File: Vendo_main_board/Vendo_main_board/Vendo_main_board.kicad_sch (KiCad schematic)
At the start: 8 parts, among them J1 Screw_Terminal_01x12, J2 Screw_Terminal_01x12, J3 Screw_Terminal_01x12, J4 Screw_Terminal_01x12

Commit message: -
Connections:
- net GNDPWR: now reaches J2.10 (Pin_10)
- net VIN+_REL_IN: now reaches J2.9 (Pin_9)
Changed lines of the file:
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@@
 		(color 0 0 0 0)
 	)
+	(junction
+		(at 302.827 226.1684)
+		(diameter 0)
+		(color 0 0 0 0)
+	)
 	(wire
 		(pts
@@
 	(wire
 		(pts
+			(xy 302.827 230.6876) (xy 302.827 226.1684)
+		)
+		(stroke
+			(width 0)
+			(type default)
+		)
+	)
+	(wire
+		(pts
 			(xy 245.3943 121.6976) (xy 314.8592 121.6976)
 		)
@@
 	(wire
 		(pts
+			(xy 300.3877 223.5894) (xy 339.8538 223.5894)
+		)
+		(stroke
+			(width 0)
+			(type default)
+		)
+	)
+	(wire
+		(pts
 			(xy 247.3131 77.6973) (xy 256.799 77.6973)
 		)
@@
 	(wire
 		(pts
+			(xy 302.827 226.1684) (xy 339.8538 226.1684)
+		)
+		(stroke
+			(width 0)
+			(type default)
+		)
+	)
+	(wire
+		(pts
 			(xy 193.24 61.42) (xy 193.24 104.1775)
 		)
@@
 	(wire
 		(pts
+			(xy 339.8538 226.1684) (xy 339.8538 226.1294)
+		)
+		(stroke
+			(width 0)
+			(type default)
+		)
+	)
+	(wire
+		(pts
 			(xy 341.3816 135.5405) (xy 341.3816 160.8719)
 		)
@@
 	(wire
 		(pts
+			(xy 300.4001 226.1684) (xy 302.827 226.1684)
+		)
+		(stroke
+			(width 0)
+			(type default)
+		)
+	)
+	(wire
+		(pts
 			(xy 109.0691 96.34) (xy 113.3814 96.34)
 		)
@@
 		)
 	)
+	(global_label "VIN+_REL_IN"
+		(shape input)
+		(at 300.3877 223.5894 180)
+		(fields_autoplaced yes)
+		(effects
+			(font
+				(size 1.27 1.27)
+			)
+			(justify right)
+		)
+		(property "Intersheetrefs" "${INTERSHEET_REFS}"
+			(at 285.4886 223.5894 0)
+			(effects
+				(font
+					(size 1.27 1.27)
+				)
+				(justify right)
+				(hide yes)
+			)
+		)
+	)
 	(global_label "DIN_DRY_6"
 		(shape input)
@@
 				)
 				(justify left)
+				(hide yes)
+			)
+		)
+	)
+	(global_label "VIN-_REL_IN"
+		(shape input)
+		(at 300.4001 226.1684 180)
+		(fields_autoplaced yes)
+		(effects
+			(font
+				(size 1.27 1.27)
+			)
+			(justify right)
+		)
+		(property "Intersheetrefs" "${INTERSHEET_REFS}"
+			(at 285.501 226.1684 0)
+			(effects
+				(font
+					(size 1.27 1.27)
+				)
+				(justify right)
 				(hide yes)
 			)
@@
 					(unit 1)
 				)
+			)
+		)
+	)
+	(symbol
+		(lib_id "power:GNDPWR")
+		(at 302.827 230.6876 0)
+		(unit 1)
+		(exclude_from_sim no)
+		(in_bom yes)
+		(on_board yes)
+		(dnp no)
+		(fields_autoplaced yes)
+		(property "Reference" "#PWR016"
+			(at 302.827 235.7676 0)
+			(effects
+				(font
+					(size 1.27 1.27)
+				)
+				(hide yes)
+			)
+		)
+		(property "Value" "GNDPWR"
+			(at 302.7 234.4976 0)
+			(effects
+				(font
+					(size 1.27 1.27)
+				)
+			)
+		)
+		(property "Footprint" ""
+			(at 302.827 231.9576 0)
+			(effects
+				(font
+					(size 1.27 1.27)
+				)
+				(hide yes)
+			)
+		)
+		(property "Datasheet" ""
+			(at 302.827 231.9576 0)
+			(effects
+				(font
+					(size 1.27 1.27)
+				)
+				(hide yes)
+			)
+		)
+		(property "Description" "Power symbol creates a global label with name \"GNDPWR\" , global ground"
+			(at 302.827 230.6876 0)
+			(effects
+				(font
+					(size 1.27 1.27)
+				)
+				(hide yes)
+			)
+		)
+		(pin "1"
+		)
+		(instances
+			(project "Vendo_main_board"
+				(path "/ce68e045-3b24-4b1f-b4c3-20bce3f1de80"
+					(reference "#PWR016")
+					(unit 1)
+				)

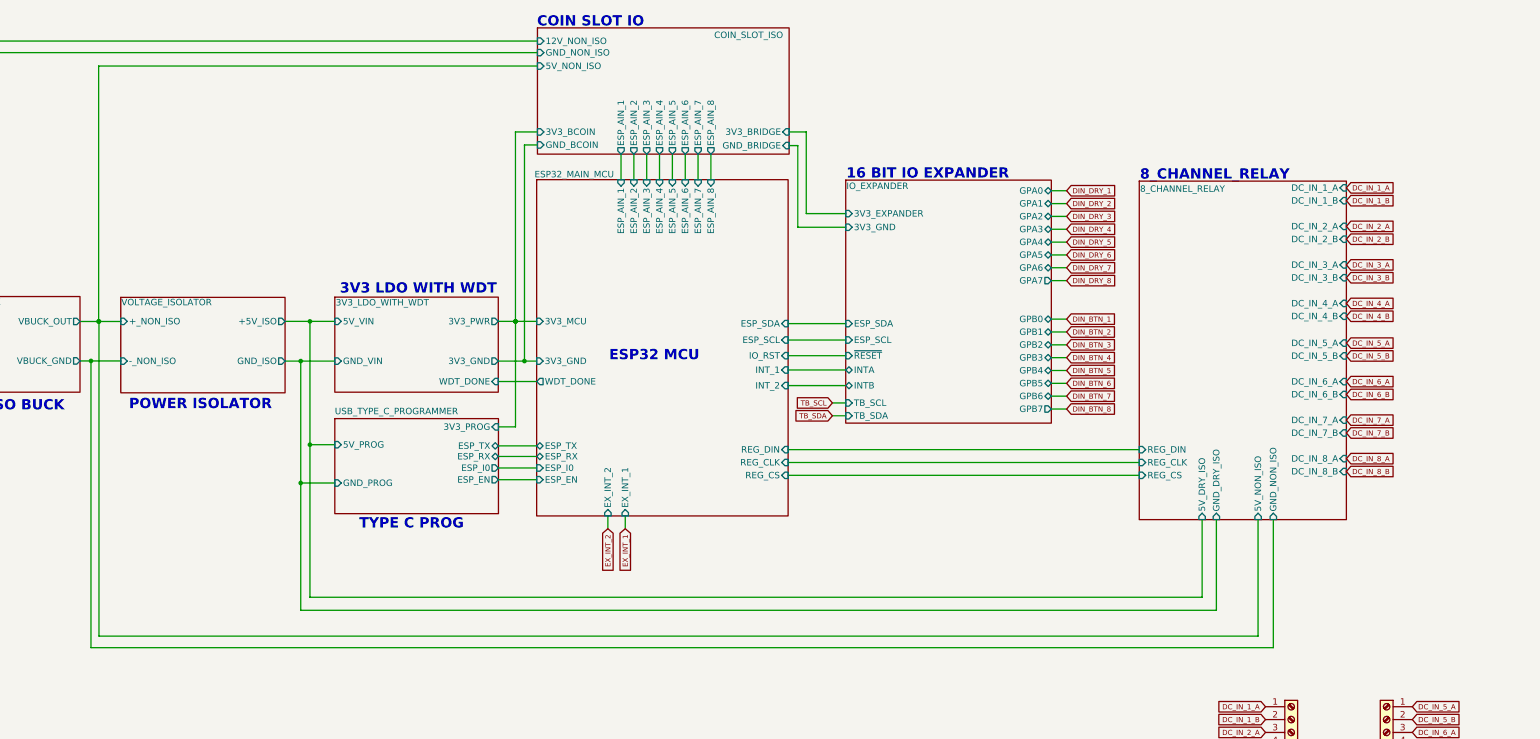
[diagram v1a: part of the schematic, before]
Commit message: -
added load switch for 12V of coin slot
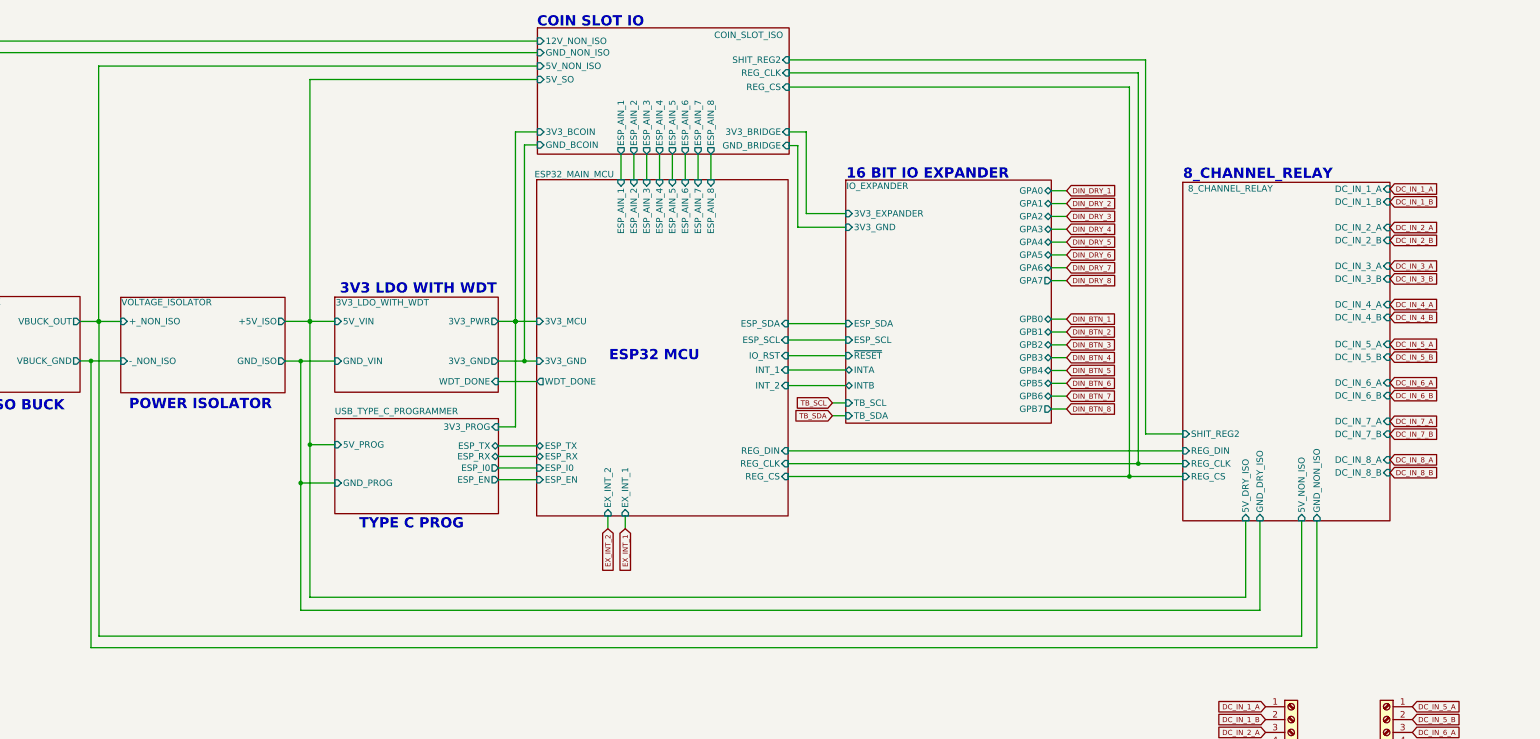
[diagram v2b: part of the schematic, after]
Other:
- sheet 8_CHANNEL_RELAY ports: added SHIT_REG2; removed none
- sheet COIN_SLOT_ISO ports: added 5V_SO, REG_CLK, REG_CS, SHIT_REG2; removed none

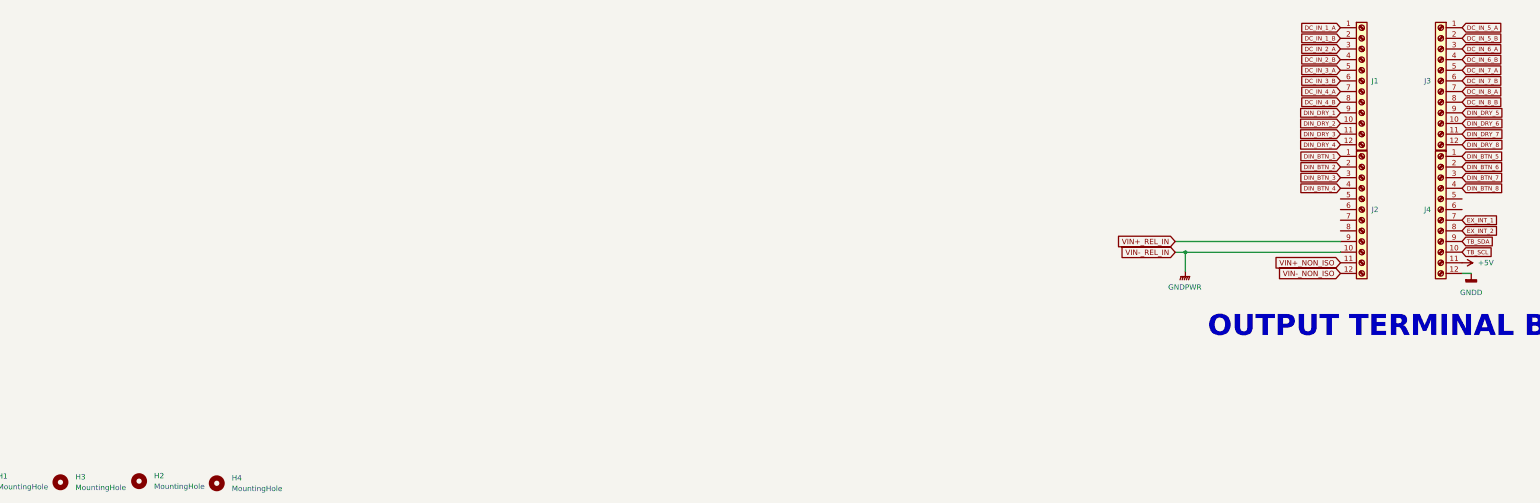
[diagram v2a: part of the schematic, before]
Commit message: -update scheme and pcb placement
update scheme and footprint
added spade connectors
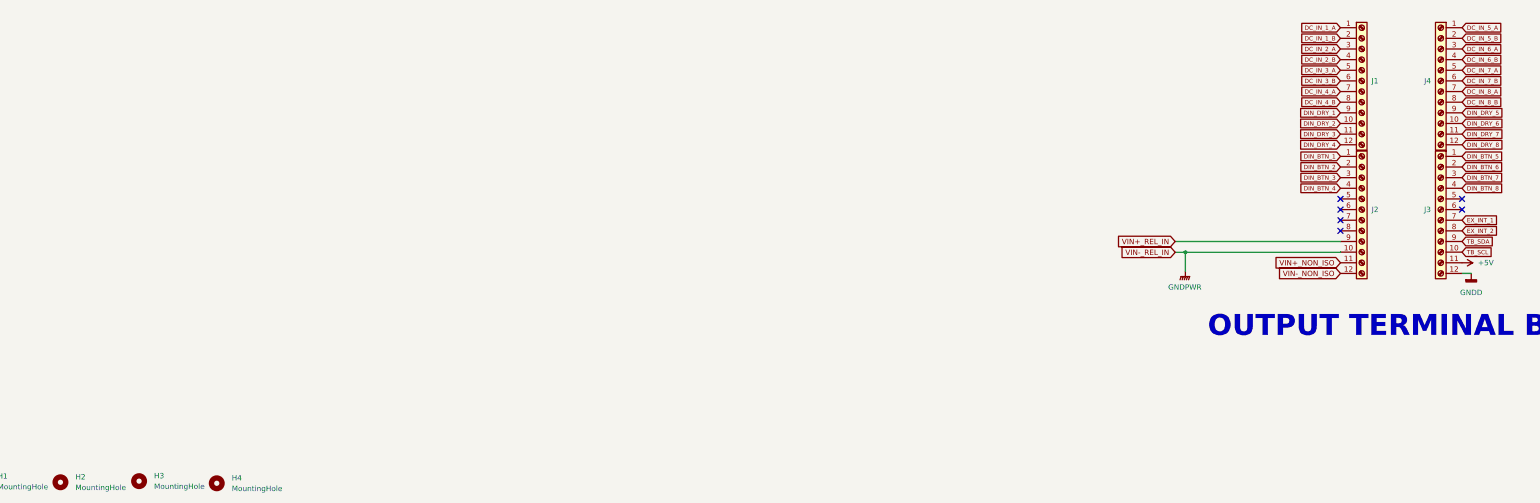
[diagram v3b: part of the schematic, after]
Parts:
- H1, H4: footprint MountingHole:MountingHole_3.2mm_M3_DIN965_Pad_TopBottom -> MountingHole:MountingHole_3.2mm_M3
- H2: renamed from H3; footprint MountingHole:MountingHole_3.2mm_M3_DIN965_Pad_TopBottom -> MountingHole:MountingHole_3.2mm_M3
- H3: renamed from H2; footprint MountingHole:MountingHole_3.2mm_M3_DIN965_Pad_TopBottom -> MountingHole:MountingHole_3.2mm_M3
- J1, J2: footprint (none) -> TerminalBlock_Phoenix:TerminalBlock_Phoenix_MKDS-1,5-12-5.08_1x12_P5.08mm_Horizontal
- J3: renamed from J4; footprint (none) -> TerminalBlock_Phoenix:TerminalBlock_Phoenix_MKDS-1,5-12-5.08_1x12_P5.08mm_Horizontal
- J4: renamed from J3; footprint (none) -> TerminalBlock_Phoenix:TerminalBlock_Phoenix_MKDS-1,5-12-5.08_1x12_P5.08mm_Horizontal
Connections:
- no-connect marks 0 -> 6
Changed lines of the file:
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@@
 		(color 0 0 0 0)
 	)
+	(no_connect
+		(at 339.8538 221.0494)
+	)
+	(no_connect
+		(at 339.8538 215.9694)
+	)
+	(no_connect
+		(at 339.8538 218.5094)
+	)
+	(no_connect
+		(at 339.8538 213.4294)
+	)
+	(no_connect
+		(at 368.867 213.4294)
+	)
+	(no_connect
+		(at 368.867 215.9694)
+	)
 	(wire
 		(pts
@@
 			)
 		)
-		(property "Footprint" ""
+		(property "Footprint" "TerminalBlock_Phoenix:TerminalBlock_Phoenix_MKDS-1,5-12-5.08_1x12_P5.08mm_Horizontal"
 			(at 344.9338 215.9694 0)
 			(effects
@@
 		(dnp no)
 		(fields_autoplaced yes)
-		(property "Reference" "#PWR0101"
+		(property "Reference" "#PWR02"
 			(at 365.057 228.6694 0)
 			(effects
@@
 			(project "Vendo_main_board"
 				(path "/ce68e045-3b24-4b1f-b4c3-20bce3f1de80"
-					(reference "#PWR0101")
+					(reference "#PWR02")
 					(unit 1)
 				)
@@
 		(dnp no)
 		(fields_autoplaced yes)
-		(property "Reference" "J3"
+		(property "Reference" "J4"
 			(at 361.448 185.2571 0)
 			(effects
@@
 			)
 		)
-		(property "Footprint" ""
+		(property "Footprint" "TerminalBlock_Phoenix:TerminalBlock_Phoenix_MKDS-1,5-12-5.08_1x12_P5.08mm_Horizontal"
 			(at 363.8031 185.2572 0)
 			(effects
@@
 			(project "Vendo_main_board"
 				(path "/ce68e045-3b24-4b1f-b4c3-20bce3f1de80"
-					(reference "J3")
+					(reference "J4")
 					(unit 1)
 				)
@@
 		(dnp no)
 		(fields_autoplaced yes)
-		(property "Reference" "#PWR016"
+		(property "Reference" "#PWR01"
 			(at 302.827 235.7676 0)
 			(effects
@@
 			(project "Vendo_main_board"
 				(path "/ce68e045-3b24-4b1f-b4c3-20bce3f1de80"
-					(reference "#PWR016")
+					(reference "#PWR01")
 					(unit 1)
 				)
@@
 			)
 		)
-		(property "Footprint" ""
+		(property "Footprint" "TerminalBlock_Phoenix:TerminalBlock_Phoenix_MKDS-1,5-12-5.08_1x12_P5.08mm_Horizontal"
 			(at 344.9177 185.2572 0)
 			(effects
@@
 			)
 		)
-		(property "Footprint" "MountingHole:MountingHole_3.2mm_M3_DIN965_Pad_TopBottom"
+		(property "Footprint" "MountingHole:MountingHole_3.2mm_M3"
 			(at 15.71 280.8873 0)
 			(effects
@@
 			)
 		)
-		(property "Footprint" "MountingHole:MountingHole_3.2mm_M3_DIN965_Pad_TopBottom"
+		(property "Footprint" "MountingHole:MountingHole_3.2mm_M3"
 			(at 71.6183 281.3039 0)
 			(effects
@@
 		(dnp no)
 		(fields_autoplaced yes)
-		(property "Reference" "H3"
+		(property "Reference" "H2"
 			(at 37.8768 279.7918 0)
 			(effects
@@
 			)
 		)
-		(property "Footprint" "MountingHole:MountingHole_3.2mm_M3_DIN965_Pad_TopBottom"
+		(property "Footprint" "MountingHole:MountingHole_3.2mm_M3"
 			(at 34.3065 281.0619 0)
 			(effects
@@
 			)
 		)
-		(property "Datasheet" "~"
+		(property "Datasheet" "MountingHole:MountingHole_3.2mm_M3"
 			(at 34.3065 281.0619 0)
 			(effects
@@
 			(project "PLC Arduino"
 				(path "/ce68e045-3b24-4b1f-b4c3-20bce3f1de80"
-					(reference "H3")
+					(reference "H2")
 					(unit 1)
 				)
@@
 		(dnp no)
 		(fields_autoplaced yes)
-		(property "Reference" "J4"
+		(property "Reference" "J3"
 			(at 361.4319 215.9693 0)
 			(effects
@@
 			)
 		)
-		(property "Footprint" ""
+		(property "Footprint" "TerminalBlock_Phoenix:TerminalBlock_Phoenix_MKDS-1,5-12-5.08_1x12_P5.08mm_Horizontal"
 			(at 363.787 215.9694 0)
 			(effects
@@
 			(project "Vendo_main_board"
 				(path "/ce68e045-3b24-4b1f-b4c3-20bce3f1de80"
-					(reference "J4")
+					(reference "J3")
 					(unit 1)
 				)
@@
 		(dnp no)
 		(fields_autoplaced yes)
-		(property "Reference" "H2"
+		(property "Reference" "H3"
 			(at 56.6476 279.523 0)
 			(effects
@@
 			)
 		)
-		(property "Footprint" "MountingHole:MountingHole_3.2mm_M3_DIN965_Pad_TopBottom"
+		(property "Footprint" "MountingHole:MountingHole_3.2mm_M3"
 			(at 53.0773 280.7931 0)
 			(effects
@@
 			(project "PLC Arduino"
 				(path "/ce68e045-3b24-4b1f-b4c3-20bce3f1de80"
-					(reference "H2")
+					(reference "H3")
 					(unit 1)
 				)
@@
 		(dnp no)
 		(fields_autoplaced yes)
-		(property "Reference" "#PWR0105"
+		(property "Reference" "#PWR03"
 			(at 371.0657 237.5594 0)
 			(effects
@@
 			(project "Vendo_main_board"
 				(path "/ce68e045-3b24-4b1f-b4c3-20bce3f1de80"
-					(reference "#PWR0105")
+					(reference "#PWR03")
 					(unit 1)
 				)
